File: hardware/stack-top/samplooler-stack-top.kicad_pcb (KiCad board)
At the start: 2 copper layers, 90 x 64 mm, 12 parts, among them J1 To bottom board, U1 OLED 0.96in, U2 INMP441

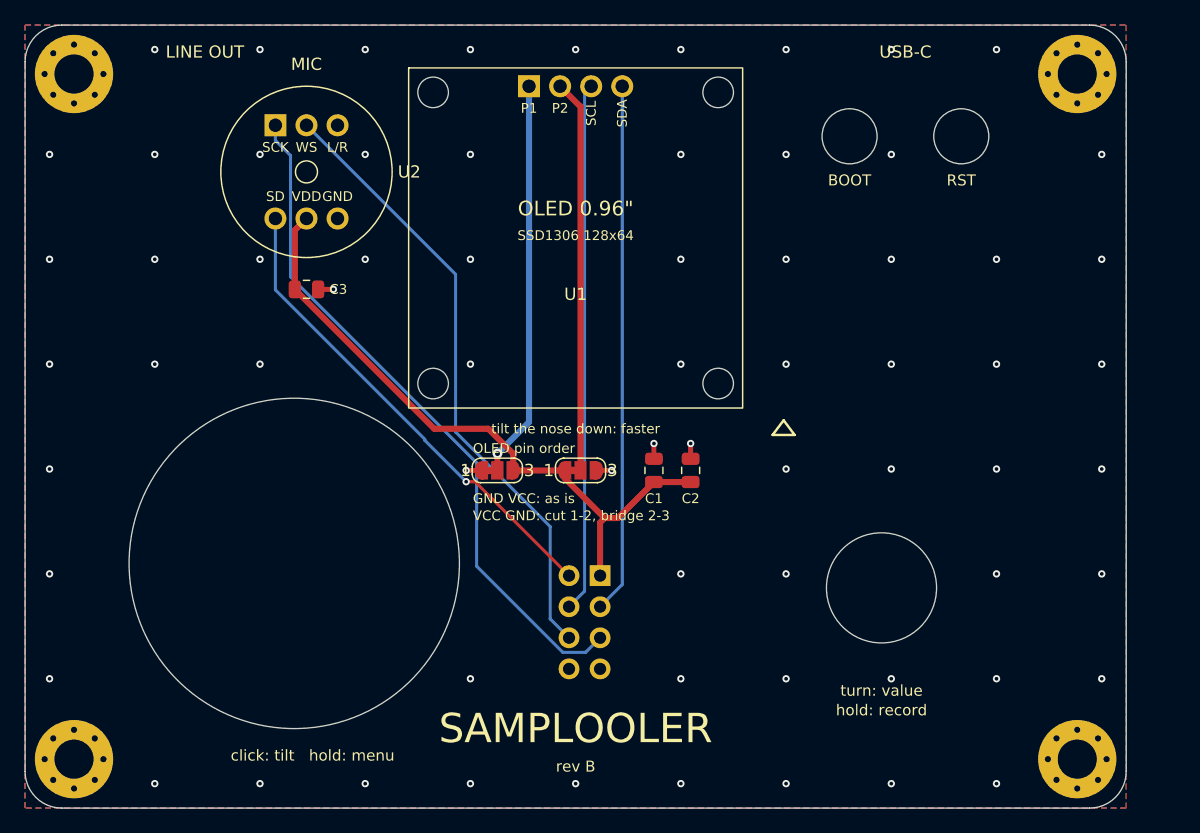
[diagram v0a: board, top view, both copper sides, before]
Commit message: Stack boards at 94 x 46 mm, one-piece JLC panels for the stack and the Mini + Filter
The stack's two boards shrink to 94 x 46 mm with the DAC straps under the
bottom board and both breakout rows in the middle, under the top board.
New hardware/gen/panel.py copies built boards onto one panel with 5 mm
tabs and mouse bites: the stack at 94 x 94 mm (panel-stack/), and the Mini
with the Samplooler Filter at 82 x 94 mm (panel-mini/), with their JLC zips,
BOM and CPL files and renders. kit.py checks router sessions for crossing
tracks of different nets before accepting them. hardware/README.md, CLAUDE.md
and the pcb-design skill describe the panels and the ordering settings.

Co-Authored-By: Claude Fable 5.1 <noreply@anthropic.com>
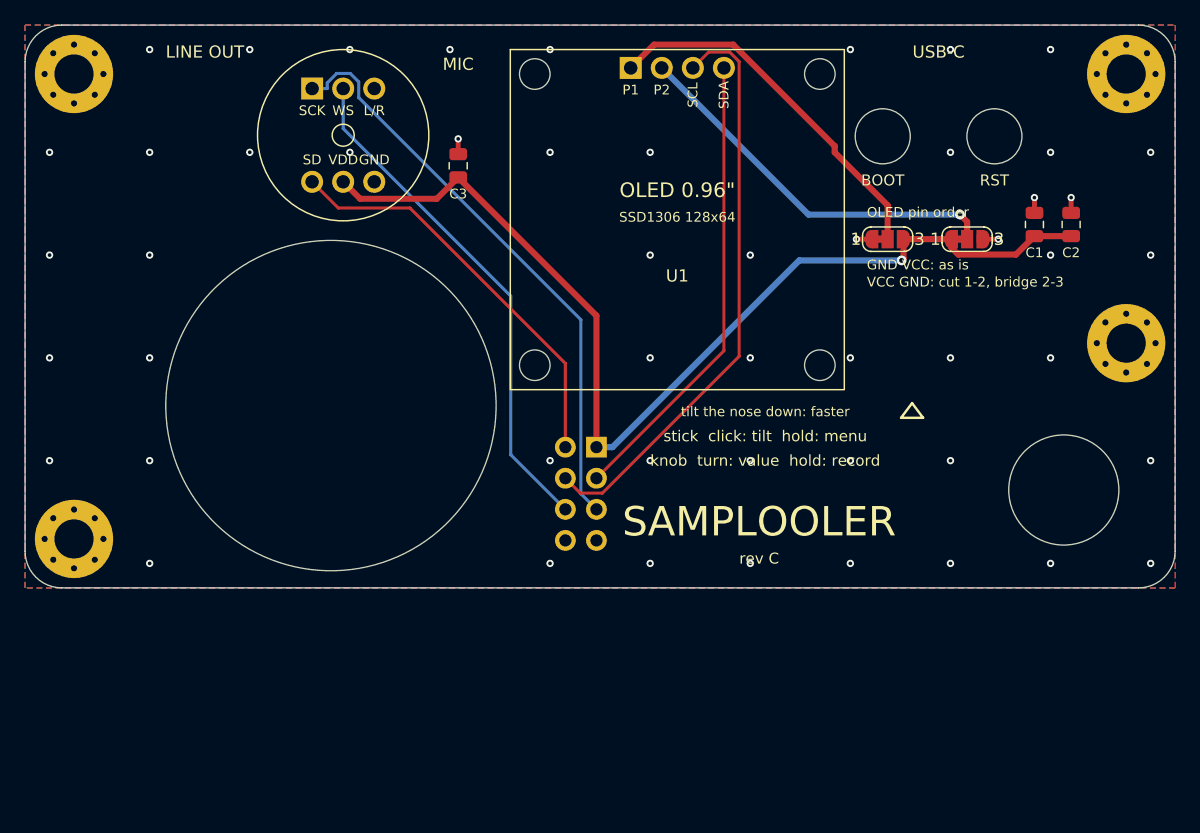
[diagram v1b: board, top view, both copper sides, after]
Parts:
- moved JP1 37.1 mm to (120.5, 67.5)
- moved C1 37.0 mm to (132.5, 66.3)
- moved C2 37.0 mm to (135.5, 66.3)
- moved JP2 36.8 mm to (127.0, 67.5)
- moved H4 34.2 mm to (140.0, 76.0)
- moved H3 18.0 mm to (54.0, 92.0)
- moved C3 16.0 mm to (85.4, 61.5), turned to 90 degrees
- moved J1 10.5 mm to (96.7, 84.5)
- moved U1 8.44 mm to (99.5, 53.5)
- moved U2 4.24 mm to (76.0, 59.0)
- moved H2 4.00 mm to (140.0, 54.0)
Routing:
- net +3V3: track 53.5 -> 85.7 mm, vias 0 -> 1
- net /I2S_WS: track 50.8 -> 41.9 mm
- net /I2S_BCLK: track 56.4 -> 47.9 mm
- net /I2S_DIN: track 39.6 -> 33.7 mm, vias 1 -> 0
- net /I2C_SDA: track 43.3 -> 37.9 mm
- net /I2C_SCL: track 43.3 -> 48.1 mm
- net /OLED_P1: track 32.5 -> 30.3 mm, vias 1 -> 0
- net /OLED_P2: track 32.1 -> 31.6 mm, vias 0 -> 1
- net GND: vias 68 -> 51
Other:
- board size 90 x 64 mm -> 94 x 46 mm
- board text added: "J1 header goes on THIS side,"
- board text added: "knob turn: value hold: record"
- board text added: "pins down"
- board text added: "rev C"
- board text added: "rev C 2026-09-28"
- board text added: "stick click: tilt hold: menu"
- board text removed: "J1 header goes on THIS side, pins down"
- board text removed: "click: tilt hold: menu"
- board text removed: "hold: record"
- board text removed: "rev B"
- board text removed: "rev B 2026-09-25"
- board text removed: "turn: value"

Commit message: Rev D boards, firmware and page changes (work in progress, before the launch cleanup)
Co-Authored-By: Claude Opus 5.5 <noreply@anthropic.com>
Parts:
- U1: value OLED 0.96in -> OLED 0.96in (under); footprint samplooler:SSD1306_0.96in_I2C -> samplooler:SSD1306_0.96in_I2C_Under; moved to B.Cu
- U2: value INMP441 -> INMP441 (under); footprint samplooler:INMP441_Round -> samplooler:INMP441_Round_Under; moved to B.Cu
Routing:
- net /OLED_P1: track 30.3 -> 48.2 mm, vias 0 -> 1
- net /I2C_SDA: track 37.9 -> 52.4 mm
- net /OLED_P2: track 31.6 -> 35.7 mm
- net +3V3: track 85.7 -> 82.9 mm, vias 1 -> 0
- net /I2C_SCL: track 48.1 -> 49.5 mm
- net /I2S_WS: track 41.9 -> 43.1 mm
- net /I2S_BCLK: track 47.9 -> 47.0 mm
- net GND: vias 51 -> 44
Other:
- outline, holes or cut-outs redrawn
- board text added: "J1 header goes on THIS side, pins down"
- board text added: "MIC: flush, sound hole up over the port"
- board text added: "OLED: header plastic on the glass side"
- board text added: "hold: freeze the tilt"
- board text added: "knob tap: menu turn: value"
- board text added: "rev D"
- board text added: "rev D 2026-10-15"
- board text added: "stick hold down: record"
- board text removed: "J1 header goes on THIS side,"
- board text removed: "knob turn: value hold: record"
- board text removed: "pins down"
- board text removed: "rev C"
- board text removed: "rev C 2026-09-28"
- board text removed: "stick click: tilt hold: menu"
